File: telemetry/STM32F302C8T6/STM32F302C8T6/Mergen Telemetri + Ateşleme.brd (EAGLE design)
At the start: 49.7 x 87.5 mm, 91 parts, among them J2 U.FL, Q2 IRLML6344TRPBF, Q3 IRLML6344TRPBF, U2 BMP280, U3 MPU-6050, U4 L86, U6 AMS1117-3.3, U7 AMS1117-3.3, U8 STM32F302C8T6, X1 JST-XH-04-PIN-LONG-PAD, Y2 ABM3B-26.000MHZ-10-1-U-T

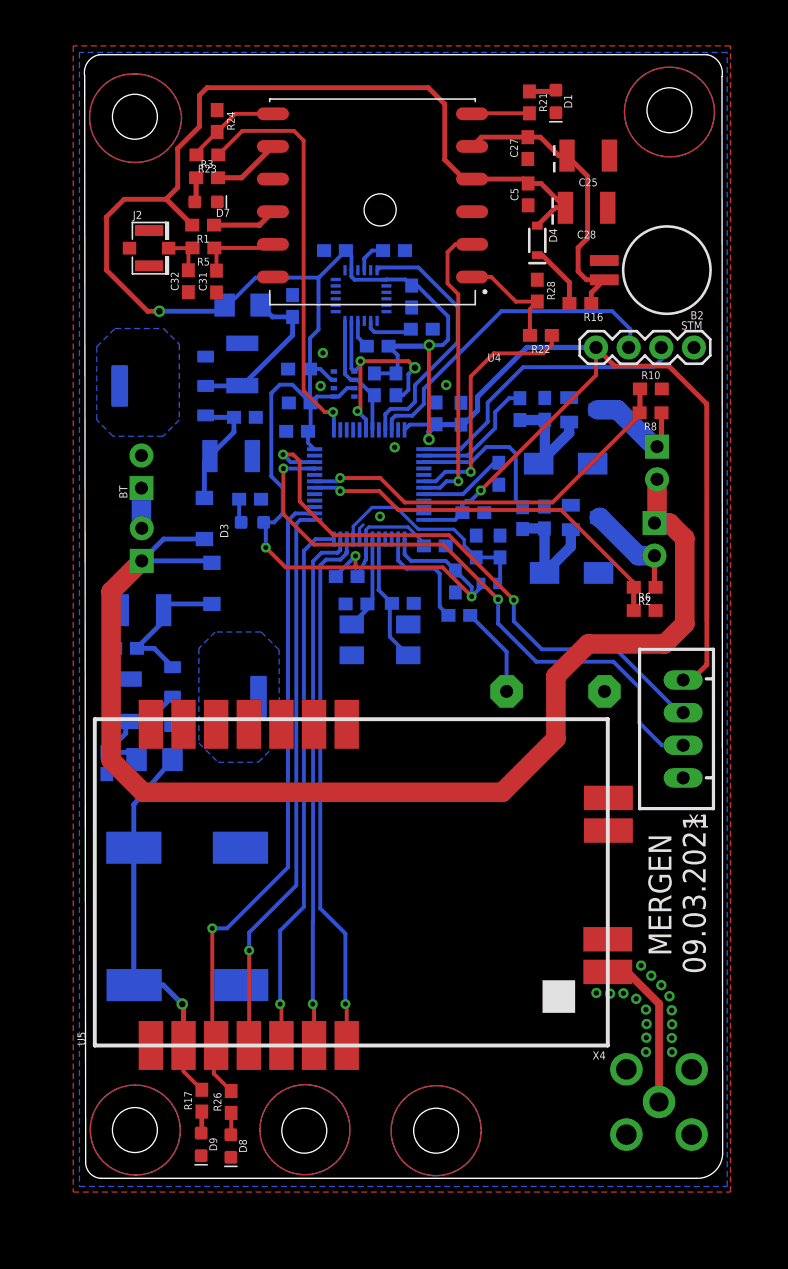
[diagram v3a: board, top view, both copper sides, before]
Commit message: Polygon 15 mils
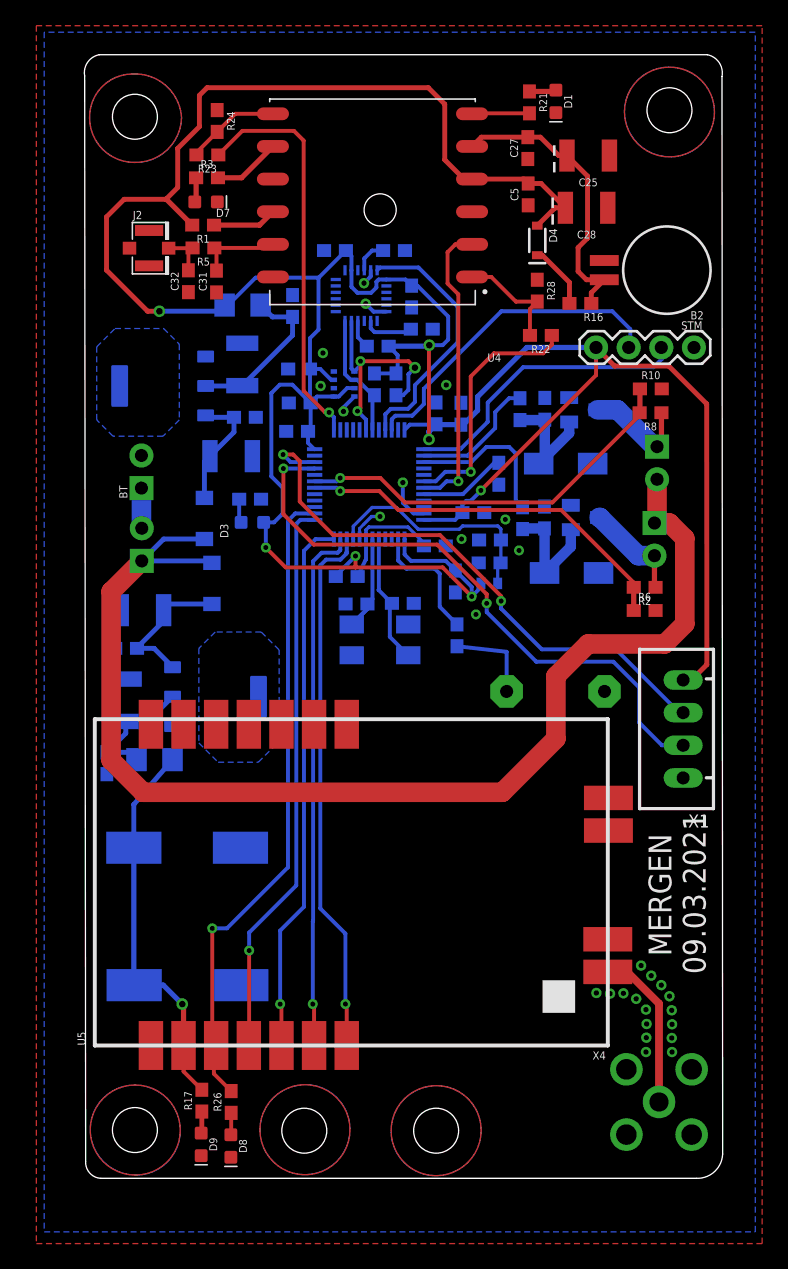
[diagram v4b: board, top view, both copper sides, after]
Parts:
- moved VDDA4 1.64 mm to (66.0, 25.9), turned to 0 degrees
- moved R7 1.56 mm to (63.5, 20.3), turned to 90 degrees
- moved VDDA3 0.94 mm to (66.1, 27.7), turned to 0 degrees
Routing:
- net GND: track 1.25 -> 11.0 mm, vias 21 -> 28
- net 3.3V: track 251.4 -> 252.9 mm
- net VDDA: track 17.0 -> 18.3 mm
- net BZZR: track 8.85 -> 9.82 mm
